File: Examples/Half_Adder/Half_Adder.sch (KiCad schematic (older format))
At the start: 7 parts, among them U1 adc_bridge_2, U2 dac_bridge_2, X1 half_adder

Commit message: Modified Example
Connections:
- net labels removed: 1, 2, 3, 4
- wire segments 40 -> 35
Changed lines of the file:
@@
 EESchema Schematic File Version 2
+LIBS:eSim_Analog
+LIBS:eSim_Devices
+LIBS:eSim_Digital
+LIBS:eSim_Hybrid
+LIBS:eSim_Miscellaneous
+LIBS:eSim_Sources
+LIBS:eSim_Subckt
+LIBS:eSim_User
+LIBS:Half_Adder-rescue
 LIBS:power
 LIBS:device
@@
 LIBS:memory
 LIBS:xilinx
-LIBS:special
 LIBS:microcontrollers
 LIBS:dsp
@@
 LIBS:contrib
 LIBS:valves
-LIBS:eSim_Analog
-LIBS:eSim_Devices
-LIBS:eSim_Digital
-LIBS:eSim_Hybrid
-LIBS:eSim_Sources
-LIBS:eSim_Subckt
 LIBS:Half_Adder-cache
 EELAYER 25 0
@@
 $EndComp
 $Comp
-L GND #PWR01
+L GND-RESCUE-Half_Adder #PWR01
 U 1 1 558A93BB
 P 2950 4000
@@
 $EndComp
 $Comp
-L GND #PWR02
+L GND-RESCUE-Half_Adder #PWR02
 U 1 1 558A93D7
 P 2950 3250
@@
 $EndComp
 $Comp
-L R R1
-U 1 1 558A940C
-P 7850 3300
-F 0 "R1" V 7930 3300 50  0000 C CNN
-F 1 "1k" V 7850 3300 50  0000 C CNN
-F 2 "" V 7780 3300 30  0000 C CNN
-F 3 "" H 7850 3300 30  0000 C CNN
-	1    7850 3300
-	0    1    1    0
-$EndComp
-$Comp
-L R R2
-U 1 1 558A945B
-P 7850 3550
-F 0 "R2" V 7930 3550 50  0000 C CNN
-F 1 "1k" V 7850 3550 50  0000 C CNN
-F 2 "" V 7780 3550 30  0000 C CNN
-F 3 "" H 7850 3550 30  0000 C CNN
-	1    7850 3550
-	0    1    1    0
-$EndComp
-$Comp
-L GND #PWR03
+L GND-RESCUE-Half_Adder #PWR03
 U 1 1 558A9480
 P 8350 3650
@@
 Text GLabel 4100 3750 2    60   Input ~ 0
 B
-Text GLabel 5200 3250 0    60   Input ~ 0
-1
-Text GLabel 5200 3700 0    60   Input ~ 0
-2
-Text GLabel 6550 3250 2    60   Input ~ 0
-3
-Text GLabel 6550 3650 2    60   Input ~ 0
-4
 Wire Wire Line
 	4050 3150 4050 3250
@@
 Connection ~ 3950 3750
 Wire Wire Line
-	5200 3700 5300 3700
-Connection ~ 5300 3700
-Wire Wire Line
-	5200 3250 5250 3250
-Wire Wire Line
-	5250 3250 5250 3450
-Connection ~ 5250 3450
-Wire Wire Line
-	6550 3250 6450 3250
-Connection ~ 6450 3250
-Wire Wire Line
-	6550 3650 6450 3650
-Connection ~ 6450 3650
-Wire Wire Line
 	7600 3750 7650 3750
 Wire Wire Line
@@
 	7650 3150 7650 3300
 Connection ~ 7650 3300
+$Comp
+L R R1
+U 1 1 55D44B20
+P 7800 3350
+F 0 "R1" H 7850 3480 50  0000 C CNN
+F 1 "1k" H 7850 3400 50  0000 C CNN
+F 2 "" H 7850 3330 30  0000 C CNN
+F 3 "" V 7850 3400 30  0000 C CNN
+	1    7800 3350
+	1    0    0    -1
+$EndComp
+$Comp
+L R R2
+U 1 1 55D44B67
+P 7800 3600
+F 0 "R2" H 7850 3730 50  0000 C CNN
+F 1 "1k" H 7850 3650 50  0000 C CNN
+F 2 "" H 7850 3580 30  0000 C CNN
+F 3 "" V 7850 3650 30  0000 C CNN
+	1    7800 3600
+	1    0    0    -1
+$EndComp
 $EndSCHEMATC

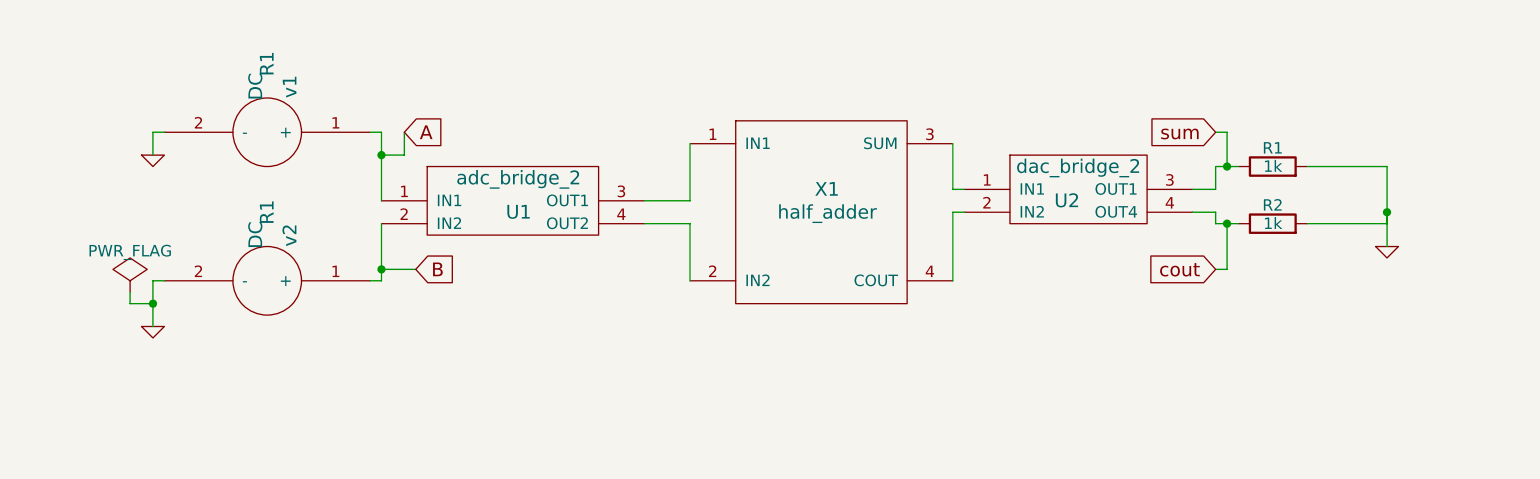
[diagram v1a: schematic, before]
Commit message: Remove unwanted example
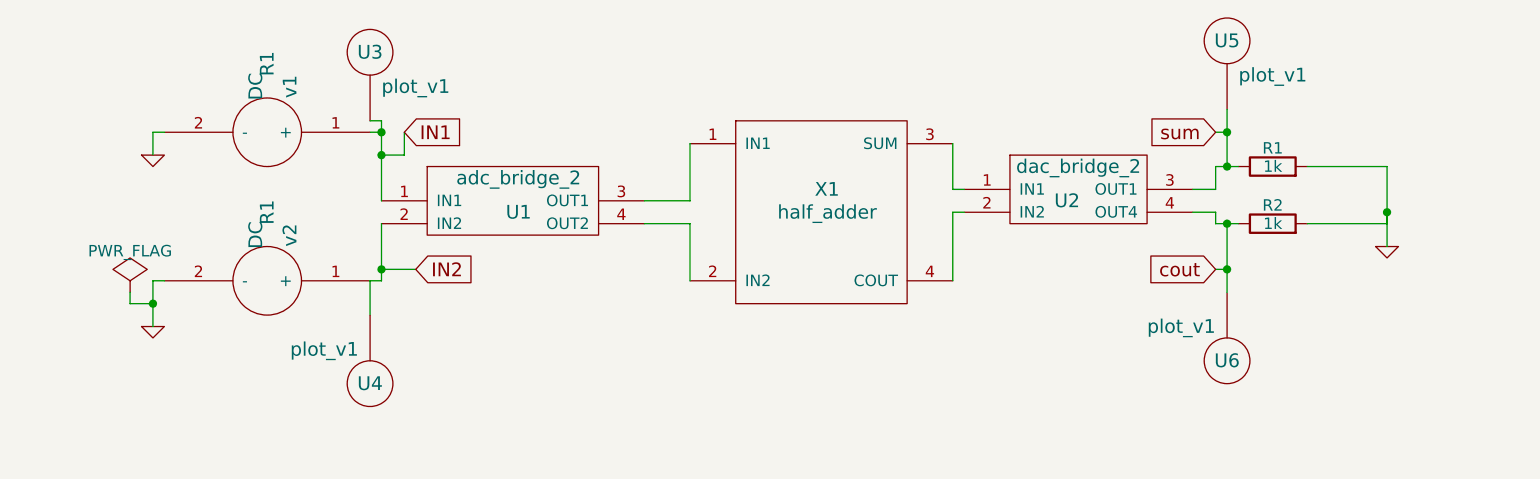
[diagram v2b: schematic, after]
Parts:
- added U3, U4, U5, U6: plot_v1, symbol plot_v1
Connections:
- net cout: now also U6.~
- net sum: now also U5.~
- net A renamed IN1
- net IN1: now also U3.~
- net B renamed IN2
- net IN2: now also U4.~
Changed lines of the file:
@@
 LIBS:eSim_Hybrid
 LIBS:eSim_Miscellaneous
+LIBS:eSim_Plot
 LIBS:eSim_Sources
 LIBS:eSim_Subckt
@@
 LIBS:contrib
 LIBS:valves
+LIBS:eSim_Power
 LIBS:Half_Adder-cache
 EELAYER 25 0
@@
 	1    0    0    -1
 $EndComp
-Wire Wire Line
-	3000 3150 2950 3150
-Wire Wire Line
-	2950 3150 2950 3250
-Wire Wire Line
-	3000 3800 2950 3800
-Wire Wire Line
-	2950 3800 2950 4000
-Wire Wire Line
-	3900 3800 3950 3800
-Wire Wire Line
-	3950 3800 3950 3550
-Wire Wire Line
-	3950 3450 3950 3150
-Wire Wire Line
-	3950 3150 3900 3150
-Wire Wire Line
-	5100 3450 5300 3450
-Wire Wire Line
-	5300 3450 5300 3200
-Wire Wire Line
-	5100 3550 5300 3550
-Wire Wire Line
-	5300 3550 5300 3800
-Wire Wire Line
-	6450 3200 6450 3400
-Wire Wire Line
-	6450 3400 6500 3400
-Wire Wire Line
-	6500 3500 6450 3500
-Wire Wire Line
-	6450 3500 6450 3800
-Wire Wire Line
-	7500 3400 7600 3400
-Wire Wire Line
-	7600 3400 7600 3300
-Wire Wire Line
-	7600 3300 7700 3300
-Wire Wire Line
-	7500 3500 7600 3500
-Wire Wire Line
-	7600 3500 7600 3550
-Wire Wire Line
-	7600 3550 7700 3550
-Wire Wire Line
-	8000 3300 8350 3300
-Wire Wire Line
-	8350 3300 8350 3650
-Wire Wire Line
-	8000 3550 8350 3550
-Wire Wire Line
-	8350 3550 8350 3500
-Connection ~ 8350 3500
 $Comp
 L PWR_FLAG #FLG04
@@
 	1    0    0    -1
 $EndComp
-Wire Wire Line
-	2850 3850 2850 3900
-Wire Wire Line
-	2850 3900 2950 3900
-Connection ~ 2950 3900
 Text GLabel 7600 3150 0    60   Input ~ 0
 sum
@@
 cout
 Text GLabel 4050 3150 2    60   Input ~ 0
-A
+IN1
 Text GLabel 4100 3750 2    60   Input ~ 0
-B
-Wire Wire Line
-	4050 3150 4050 3250
-Wire Wire Line
-	4050 3250 3950 3250
-Connection ~ 3950 3250
-Wire Wire Line
-	4100 3750 3950 3750
-Connection ~ 3950 3750
-Wire Wire Line
-	7600 3750 7650 3750
-Wire Wire Line
-	7650 3750 7650 3550
-Connection ~ 7650 3550
-Wire Wire Line
-	7600 3150 7650 3150
-Wire Wire Line
-	7650 3150 7650 3300
-Connection ~ 7650 3300
+IN2
 $Comp
 L R R1
@@
 	1    0    0    -1
 $EndComp
+$Comp
+L plot_v1 U3
+U 1 1 56D860CB
+P 3900 3300
+F 0 "U3" H 3900 3800 60  0000 C CNN
+F 1 "plot_v1" H 4100 3650 60  0000 C CNN
+F 2 "" H 3900 3300 60  0000 C CNN
+F 3 "" H 3900 3300 60  0000 C CNN
+	1    3900 3300
+	1    0    0    -1
+$EndComp
+$Comp
+L plot_v1 U4
+U 1 1 56D8619C
+P 3900 3750
+F 0 "U4" H 3900 4250 60  0000 C CNN
+F 1 "plot_v1" H 4100 4100 60  0000 C CNN
+F 2 "" H 3900 3750 60  0000 C CNN
+F 3 "" H 3900 3750 60  0000 C CNN
+	1    3900 3750
+	-1   0    0    1
+$EndComp
+$Comp
+L plot_v1 U5
+U 1 1 56D8629D
+P 7650 3250
+F 0 "U5" H 7650 3750 60  0000 C CNN
+F 1 "plot_v1" H 7850 3600 60  0000 C CNN
+F 2 "" H 7650 3250 60  0000 C CNN
+F 3 "" H 7650 3250 60  0000 C CNN
+	1    7650 3250
+	1    0    0    -1
+$EndComp
+$Comp
+L plot_v1 U6
+U 1 1 56D86375
+P 7650 3650
+F 0 "U6" H 7650 4150 60  0000 C CNN
+F 1 "plot_v1" H 7850 4000 60  0000 C CNN
+F 2 "" H 7650 3650 60  0000 C CNN
+F 3 "" H 7650 3650 60  0000 C CNN
+	1    7650 3650
+	-1   0    0    1
+$EndComp
+Wire Wire Line
+	3000 3150 2950 3150
+Wire Wire Line
+	2950 3150 2950 3250
+Wire Wire Line
+	3000 3800 2950 3800
+Wire Wire Line
+	2950 3800 2950 4000
+Wire Wire Line
+	3900 3800 3950 3800
+Wire Wire Line
+	3950 3800 3950 3550
+Wire Wire Line
+	3950 3100 3950 3450
+Wire Wire Line
+	3950 3150 3900 3150
+Wire Wire Line
+	5100 3450 5300 3450
+Wire Wire Line
+	5300 3450 5300 3200
+Wire Wire Line
+	5100 3550 5300 3550
+Wire Wire Line
+	5300 3550 5300 3800
+Wire Wire Line
+	6450 3200 6450 3400
+Wire Wire Line
+	6450 3400 6500 3400
+Wire Wire Line
+	6500 3500 6450 3500
+Wire Wire Line
+	6450 3500 6450 3800
+Wire Wire Line
+	7500 3400 7600 3400
+Wire Wire Line
+	7600 3400 7600 3300
+Wire Wire Line
+	7600 3300 7700 3300
+Wire Wire Line
+	7500 3500 7600 3500
+Wire Wire Line
+	7600 3500 7600 3550
+Wire Wire Line
+	7600 3550 7700 3550
+Wire Wire Line
+	8000 3300 8350 3300
+Wire Wire Line
+	8350 3300 8350 3650
+Wire Wire Line
+	8000 3550 8350 3550
+Wire Wire Line
+	8350 3550 8350 3500
+Connection ~ 8350 3500
+Wire Wire Line
+	2850 3850 2850 3900
+Wire Wire Line
+	2850 3900 2950 3900
+Connection ~ 2950 3900
+Wire Wire Line
+	4050 3150 4050 3250
+Wire Wire Line
+	4050 3250 3950 3250
+Connection ~ 3950 3250
+Wire Wire Line
+	4100 3750 3950 3750
+Connection ~ 3950 3750
+Wire Wire Line
+	7600 3750 7650 3750
+Wire Wire Line
+	7650 3550 7650 3850
+Connection ~ 7650 3550
+Wire Wire Line
+	7600 3150 7650 3150
+Wire Wire Line
+	7650 3050 7650 3300
+Connection ~ 7650 3300
+Connection ~ 7650 3750
+Connection ~ 7650 3150
+Wire Wire Line
+	3950 3100 3900 3100
+Connection ~ 3950 3150
+Wire Wire Line
+	3900 3950 3900 3800
 $EndSCHEMATC
